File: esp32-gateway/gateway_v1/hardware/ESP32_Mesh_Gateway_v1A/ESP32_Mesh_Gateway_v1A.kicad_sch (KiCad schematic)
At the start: 12 parts, among them J1 Ext Power, U1 ESP32-S3 Super Mini, U2 ESP32-C3 Super Mini, U3 BME280

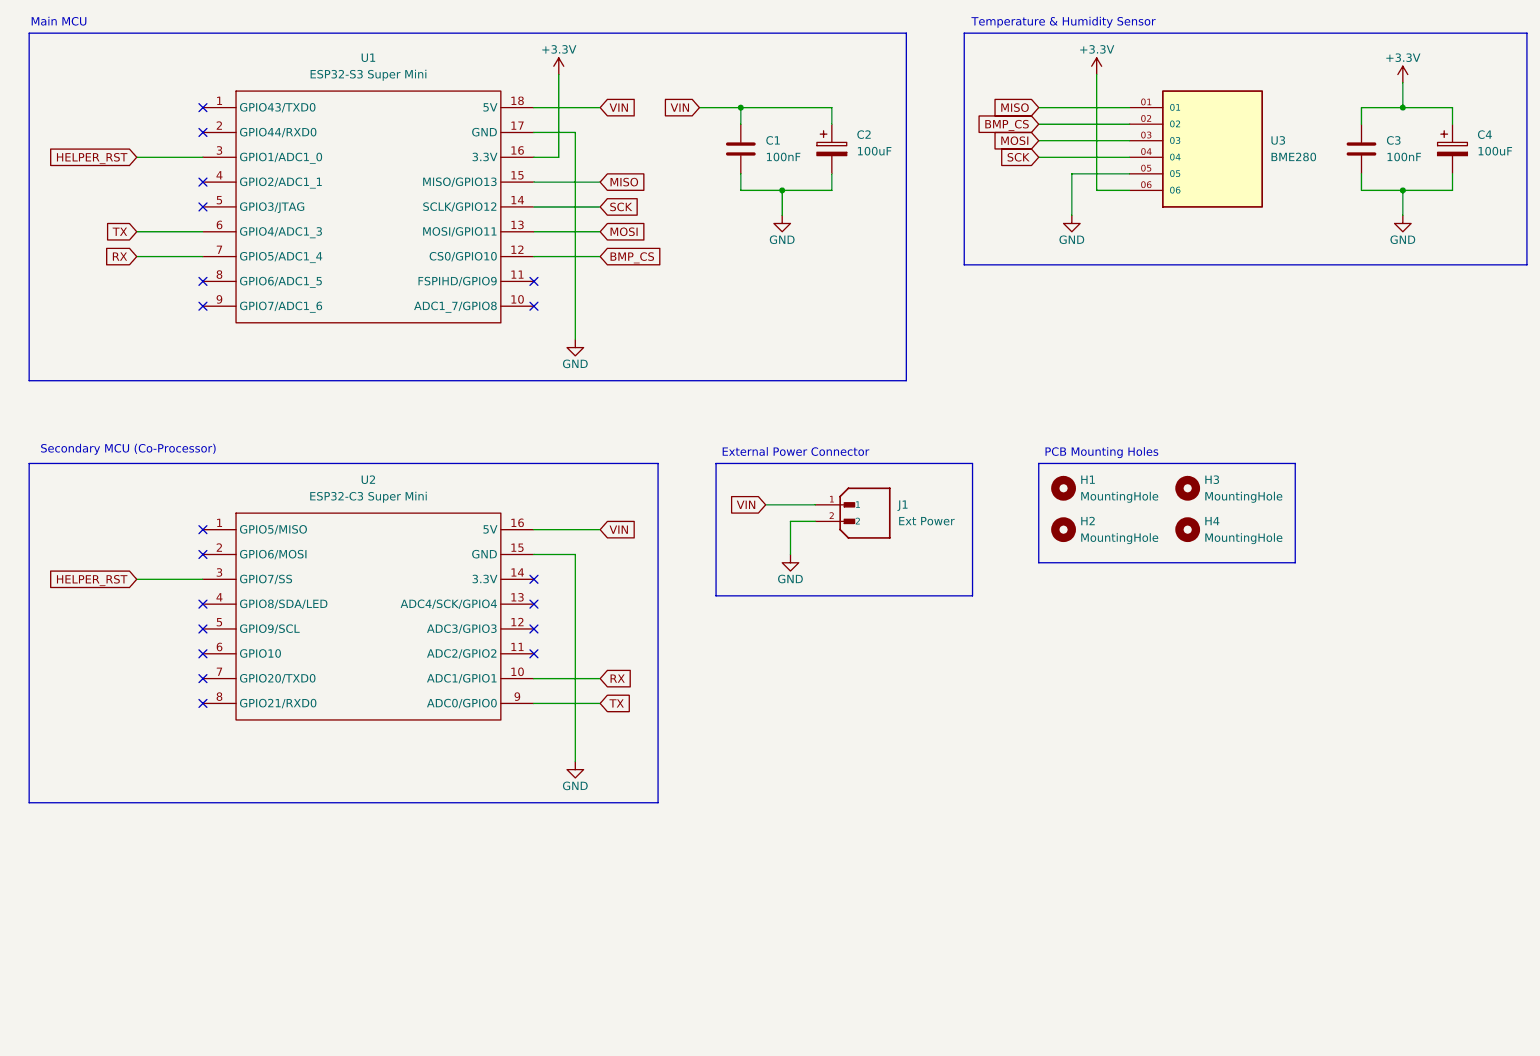
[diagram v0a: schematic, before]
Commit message: feat: improve node discovery, add new gateway PCB variants, and document C3 Super Mini RF fixes
- polish gateway and node discovery behavior so pairing candidates appear faster and stale "available to pair" entries clear more predictably
- document the new Gateway v1A-v1D single-layer THT PCB variants for these board combinations:
  - v1A: Seeed Studio XIAO ESP32-S3 + ESP32-C3 Super Mini
  - v1B: Seeed Studio XIAO ESP32-S3 + Seeed Studio XIAO ESP32-C3
  - v1C: Seeed Studio XIAO ESP32-S3 + DFRobot Beetle ESP32-C3
  - v1D: Waveshare ESP32-S3-DevKit-C-N8R8 + ESP32-C3 Super Mini
- note that all new gateway PCB variants include connection points for a future BME280 module
- deprecate the earlier ESP32-S3 Super Mini based gateway PCB because its 4 MB flash is not suitable for the current gateway firmware line
- document the introduction of user_config.h as the new home for user-configurable firmware definitions across gateway and node projects
- document the ESP32-C3 Super Mini specific WiFi transmit power limit behavior and note that it must be applied only after WiFi startup
- bump documented firmware versions:
  - gateway main firmware: v2.1.4 -> v2.2.0
  - gateway coprocessor firmware: v0.1.1 -> v0.2.0
  - sensor node firmware: v2.1.4 -> v2.2.0
  - relay node firmware: v1.2.2 -> v1.3.0
  - hybrid relay node firmware: v0.1.3 -> v0.2.0
  - user_config.h: v1.0.0 introduced
- add a dedicated ESP32-C3 Super Mini WiFi test report with the full receive/transmit test tables from Test-1 to Test-12
- summarize the documented RF findings:
  - some Super Mini boards had weak or unstable onboard LDOs
  - stock ceramic antenna performance was poor
  - LDO replacement and antenna changes improved several boards
  - the 8.5 dBm TX cap helped stabilize marginal boards
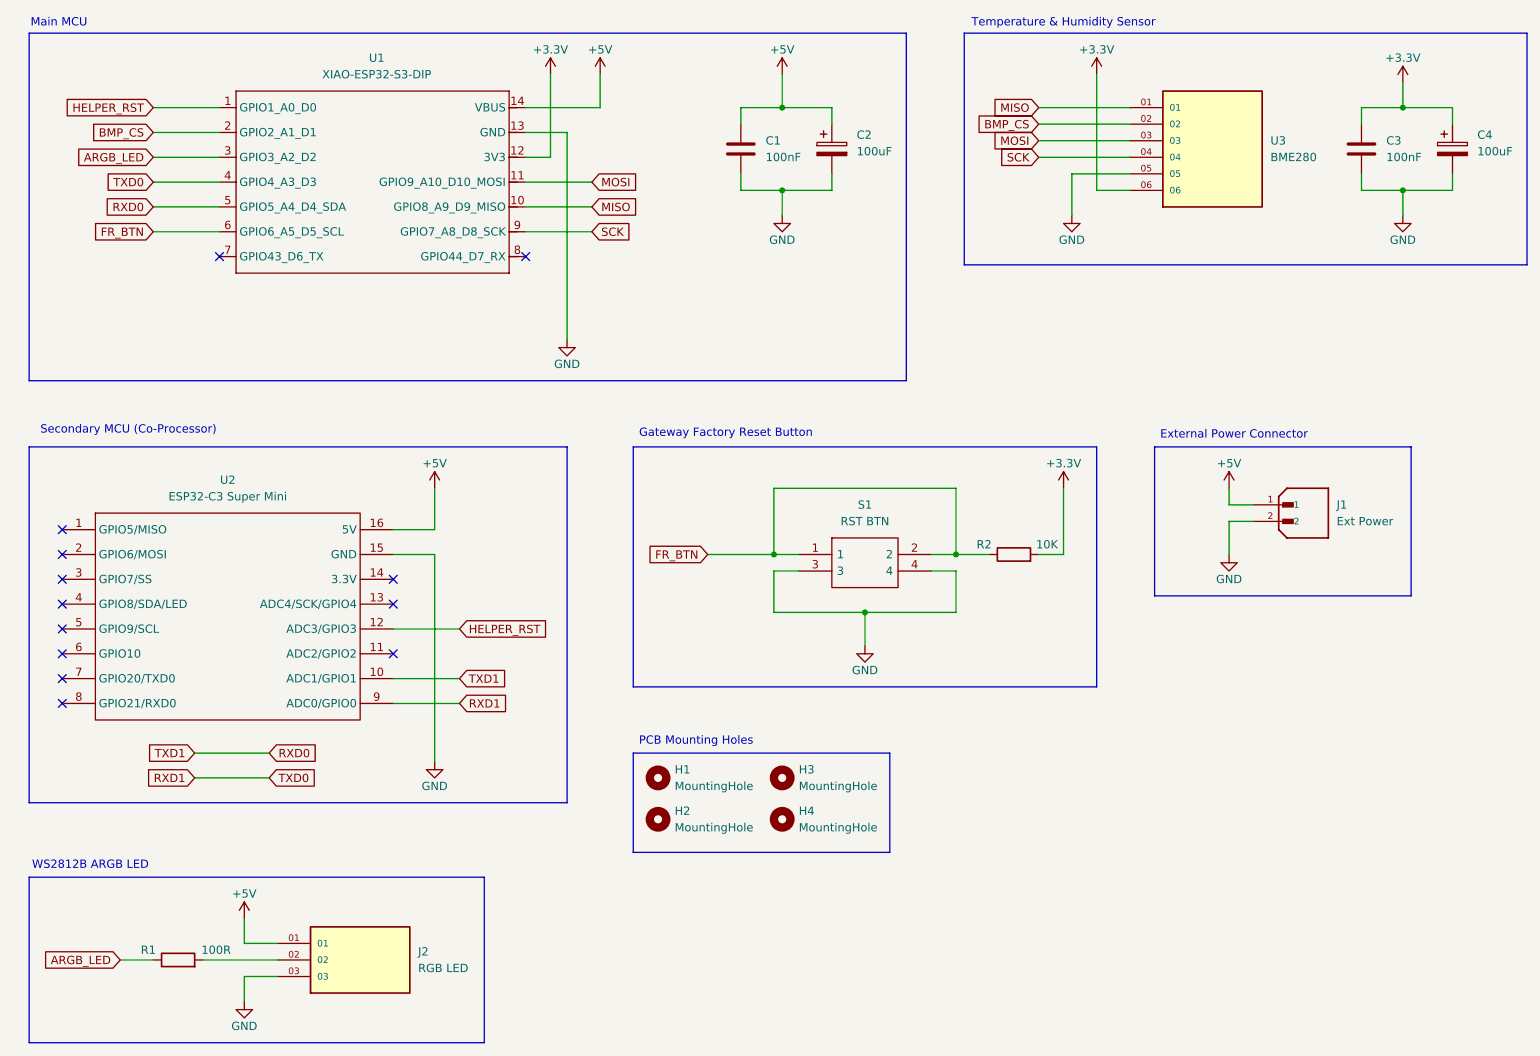
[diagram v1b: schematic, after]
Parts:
- removed U1: ESP32-S3 Super Mini, Development_Boards:ESP32-S3_Super_Mini, symbol Development_Boards:ESP32-S3_Super_Mini
- added J2: RGB LED, TSW-103-07-G-S:SAMTEC_TSW-103-07-G-S, symbol TSW-103-07-G-S:TSW-103-07-G-S
- added R1: 100R, Resistor_THT:R_Axial_DIN0207_L6.3mm_D2.5mm_P10.16mm_Horizontal, symbol Device:R
- added R2: 10K, Resistor_THT:R_Axial_DIN0207_L6.3mm_D2.5mm_P10.16mm_Horizontal, symbol Device:R
- added S1: RST BTN, FSM10JH:FSM4JH, symbol FSM10JH:FSM10JH
- added U1: XIAO-ESP32-S3-DIP, XIAO_Series_Boards:Xiao ESP32-S3 THT, symbol Seeed_Studio_XIAO_Series:XIAO-ESP32-S3-DIP
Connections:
- net +3.3V: now also R2.2, U1.12 (3V3)
- net BMP_CS: now also U1.2 (GPIO2_A1_D1)
- net GND: now also J2.03, S1.3, S1.4, U1.13 (GND)
- net HELPER_RST: now also U2.12 (ADC3/GPIO3), U1.1 (GPIO1_A0_D0); no longer U2.3 (GPIO7/SS)
- net MISO: now also U1.10 (GPIO8_A9_D9_MISO)
- net MOSI: now also U1.11 (GPIO9_A10_D10_MOSI)
- net SCK: now also U1.9 (GPIO7_A8_D8_SCK)
- net RX renamed RXD0
- net RXD0: now also U1.5 (GPIO5_A4_D4_SDA)
- net TX renamed RXD1
- net RXD1: now also U1.4 (GPIO4_A3_D3)
- net VIN renamed +5V
- net +5V: now also J2.01, U1.14 (VBUS)
- new net: J2.02, R1.2
- new net ARGB_LED: R1.1, U1.3 (GPIO3_A2_D2)
- new net FR_BTN: R2.1, S1.1, S1.2, U1.6 (GPIO6_A5_D5_SCL)
- no-connect marks 19 -> 13
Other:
- note added: "Gateway Factory Reset Button"
- note added: "WS2812B ARGB LED"
- title: ESP32 Mesh System Gateway -> ESPNow Mesh System Gateway
- moved on the sheet: H1, H2, H3, H4, J1
